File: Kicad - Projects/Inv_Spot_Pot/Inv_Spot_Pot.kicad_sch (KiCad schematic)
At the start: 68 parts, among them J1 Screw_Terminal_01x03, J2 PWM, J3 Display_Power, J4 Current_Sense, Q1 40T120, Q2 40T120, Q3 40T120, Q4 40T120, T1 Transformer_1P_1S, U2 LTV-817S

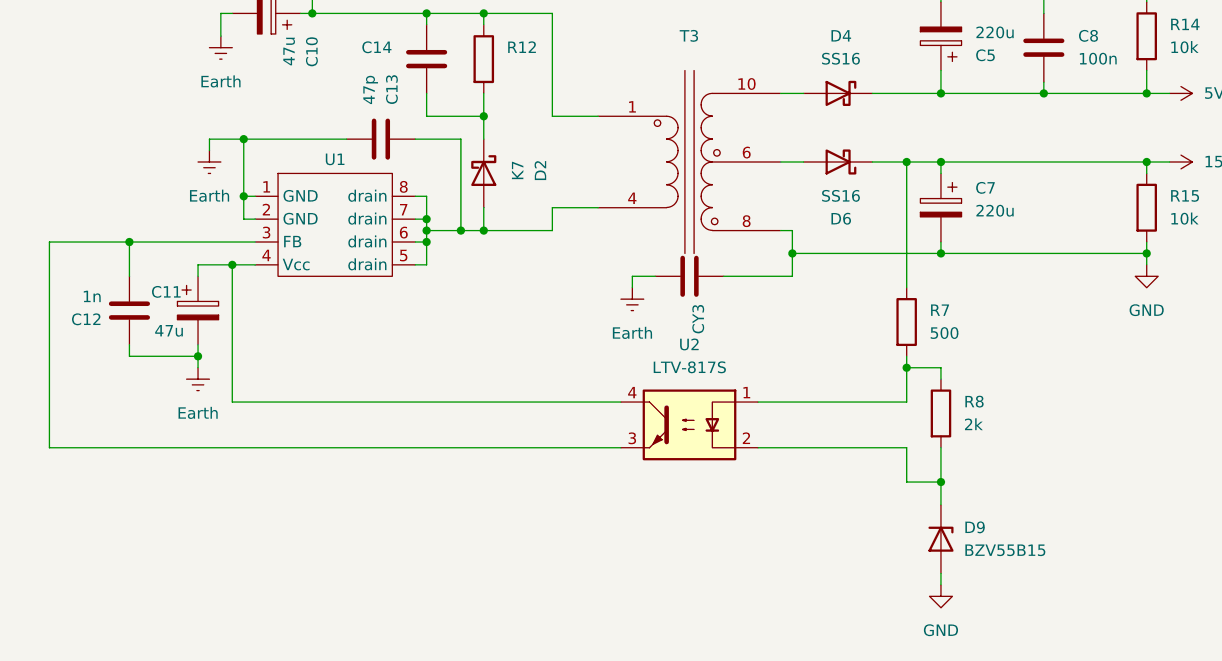
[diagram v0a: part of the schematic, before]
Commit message: Ajuste da PCB
Alargamento das trilhas T- e T+ por meio de zonas de cobre

Ajuste do circuito da fonte auxiliar para uso de zener comum ao invés de TL431
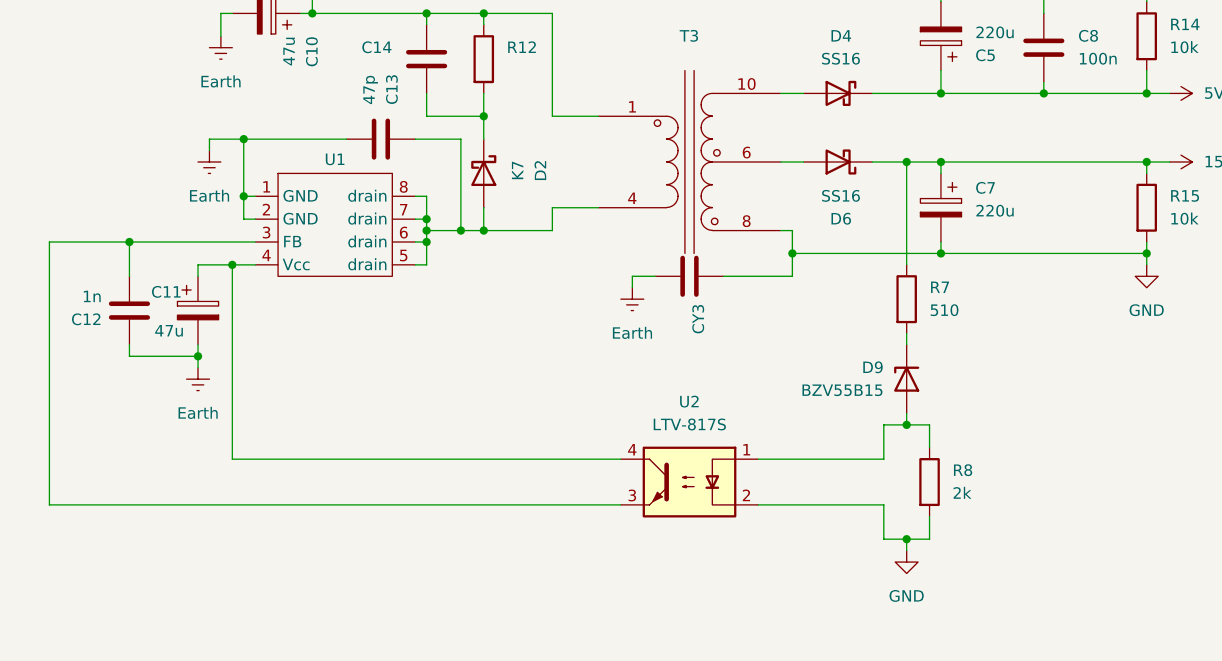
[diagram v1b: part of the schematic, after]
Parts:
- R7: value 500 -> 510
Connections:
- net GND: now also R8.2, U2.2; no longer D9.2 (A)
- net at R8.1, U2.1: now also D9.2 (A); no longer R7.2
- new net: D9.1 (K), R7.2
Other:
- moved on the sheet: D9, R7, R8, U2

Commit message: Atualizações Semi-Finais
Conexão do soft-start e filtro de entrada na placa
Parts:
- removed C10, C11: 47u, Capacitor_THT:CP_Radial_D8.0mm_P3.50mm, symbol Device:C_Polarized
- removed C12: 1n, Capacitor_SMD:C_1206_3216Metric_Pad1.33x1.80mm_HandSolder, symbol Device:C
- removed C13: 47p, Capacitor_THT:C_Disc_D8.0mm_W5.0mm_P7.50mm, symbol Device:C
- removed C14, C8, C9: 100n, Capacitor_SMD:C_1206_3216Metric_Pad1.33x1.80mm_HandSolder, symbol Device:C
- removed C5, C7: 220u, Capacitor_THT:CP_Radial_D8.0mm_P3.50mm, symbol Device:C_Polarized
- removed CY3: C, Capacitor_THT:C_Disc_D10.5mm_W5.0mm_P10.00mm, symbol Device:C
- removed D2: K7, Diode_SMD:D_SMA_Handsoldering, symbol Device:D_Schottky
- removed D4: SS16, Diode_SMD:D_SMA_Handsoldering, symbol Device:D_Schottky
- removed D6: SS16, Diode_SMD:D_SOD-128, symbol Device:D_Schottky
- removed D9: BZV55B15, Diode_SMD:D_MiniMELF, symbol Diode:BZV55B15
- removed F1: Fuse, Fuse:Fuseholder_Clip-5x20mm_Schurter_CQM_Inline_P20.60x5.00mm_D1.00mm_Horizontal, symbol Device:Fuse
- removed F2: Polyfuse, Connector_PinHeader_2.54mm:PinHeader_1x02_P2.54mm_Vertical, symbol Device:Polyfuse
- removed J4: Current_Sense, Connector_PinHeader_2.54mm:PinHeader_1x02_P2.54mm_Vertical, symbol Connector:Conn_01x02_Pin
- removed R12, R8: 2k, Resistor_SMD:R_1206_3216Metric_Pad1.30x1.75mm_HandSolder, symbol Device:R
- removed R14, R15: 10k, Resistor_SMD:R_1206_3216Metric_Pad1.30x1.75mm_HandSolder, symbol Device:R
- removed R7: 510, Resistor_SMD:R_1206_3216Metric_Pad1.30x1.75mm_HandSolder, symbol Device:R
- removed T3: (no value), Transformer_THT:Custom_Transformer-10P-EEL22_EE30_7, symbol Custom_Transformers:Transformer_1P_2S_CT
- removed TR1: TR60_FC, Transformer_THT:Current_Transformer-1_200-21x20, symbol Transformer:TR60_FC
- removed U1: (no value), Package_DIP:DIP-8_W7.62mm_LongPads, symbol Custom_ICs:DK125
- removed U2: LTV-817S, Package_DIP:SMDIP-4_W9.53mm, symbol Isolator:LTV-817S
- added C3, C4: 220u, Capacitor_THT:CP_Radial_D35.0mm_P10.00mm_SnapIn, symbol Device:C_Polarized
- added D10, D11, D12, D13, D14, D15: MUR80G20, Package_TO_SOT_THT:TO-3P-3_Vertical, symbol Device:D_Schottky_Dual_CommonCathode_KAA_Parallel
- added R22: 200k, Resistor_SMD:R_2010_5025Metric, symbol Device:R
- D1: footprint Diode_THT:Diode_Bridge_Vishay_KBU -> Diode_THT:Diode_Bridge_32.0x5.6x17.0mm_P10.0mm_P7.5mm
- J1: footprint TerminalBlock:TerminalBlock_Altech_AK300-3_P5.00mm -> (none)
- R21: footprint Resistor_SMD:R_1206_3216Metric_Pad1.30x1.75mm_HandSolder -> Resistor_SMD:R_2010_5025Metric
- RV1: footprint Varistor:RV_Disc_D21.5mm_W5.6mm_P10mm -> Varistor:RV_Disc_D21.5mm_W4.3mm_P10mm
- renumbered C6 to C2
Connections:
- net 15V: now also J3.1 (Pin_1)
- net 310V: now also C3.1, C4.1, R22.1
- net Earth: now also C3.2, C4.2, R22.2
- net T+: now also T1.1 (AA)
- net T-: now also T1.2 (AB); no longer T1.1 (AA)
- net Soft_Start-24V/~{AC{2}}: now reaches Cx1.1, FL1.1, RV1.1
- net Soft_Start-24V/~{AC{1}}: now reaches Cx1.2, FL1.3, RV1.2
- net Soft_Start-24V/~{AC{1}}: no longer J1.3 (Pin_3)
- net Soft_Start-24V/AC_{1}: now reaches J1.1 (Pin_1)
- new net: D10.2 (A), D11.2 (A), D12.2 (A), D13.2 (A), D14.2 (A), D15.2 (A)
- new net Out1: D10.1 (K), D10.3 (K), D11.1 (K), D11.3 (K), D14.1 (K), D14.3 (K)
- new net Out2: D12.1 (K), D12.3 (K), D13.1 (K), D13.3 (K), D15.1 (K), D15.3 (K)
- new net Soft_Start-24V/AC_{2}: J1.3 (Pin_3)
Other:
- added sheet Power_Supply (PS-5_15.kicad_sch)
- added sheet Soft_Start-24V (Sheets/Soft_Start.kicad_sch)
- moved on the sheet: C1, C15, C16, C17, C18, C2, CY1, CY2, Cx1, Cx2, D1, FL1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

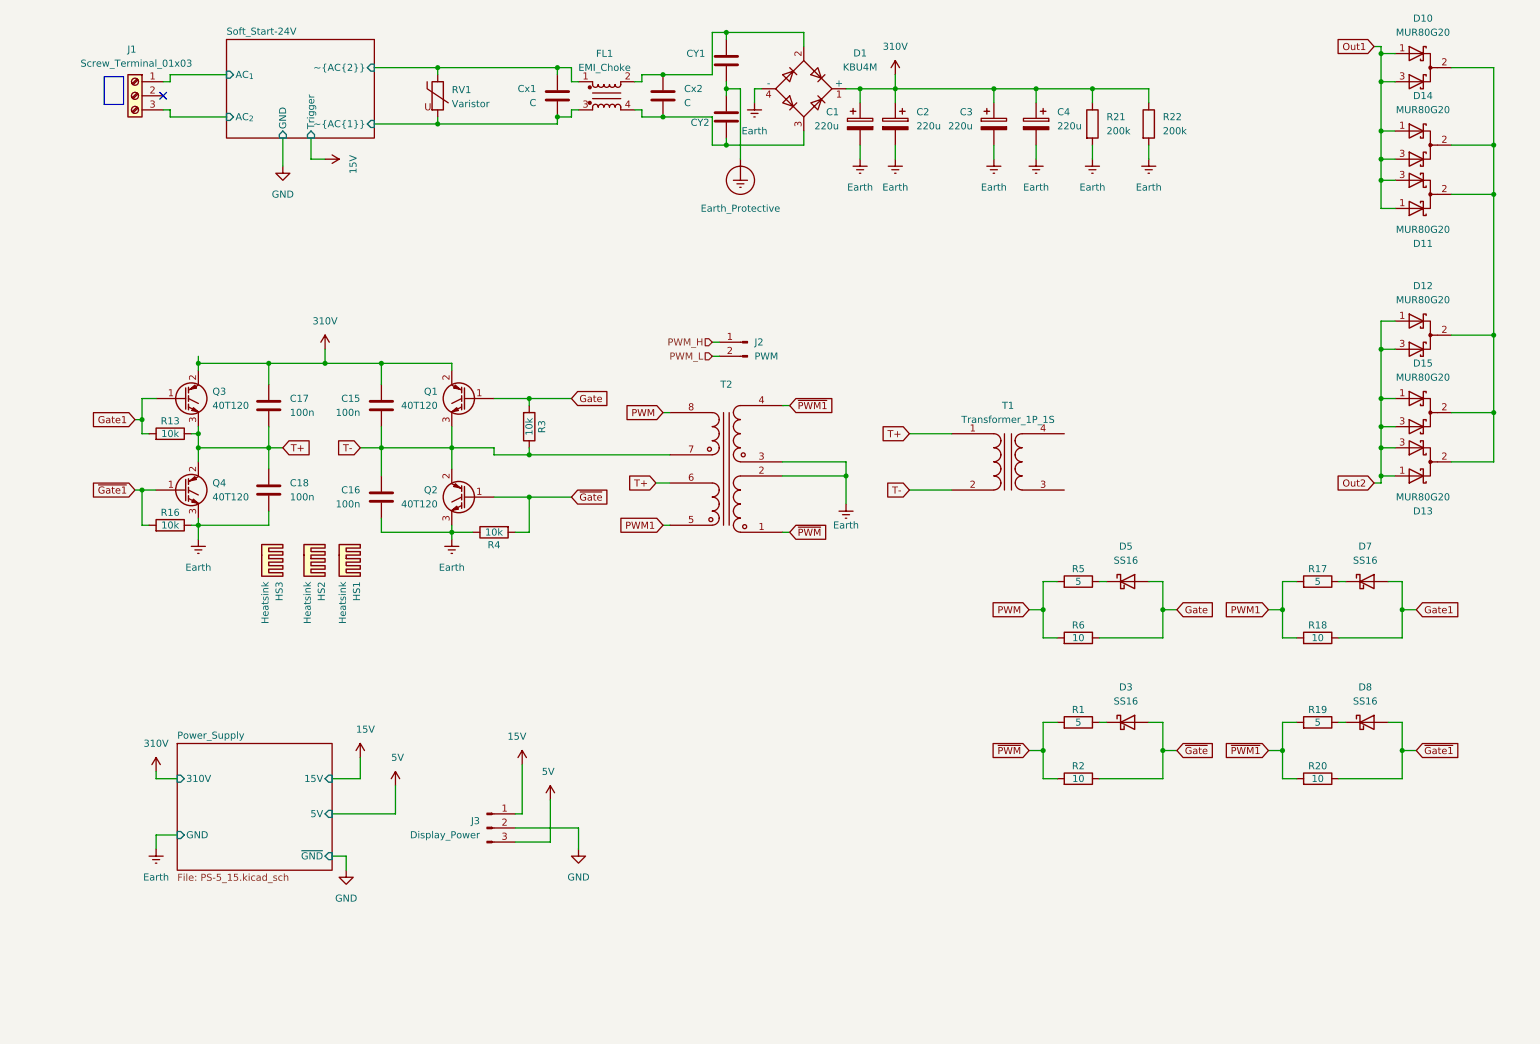
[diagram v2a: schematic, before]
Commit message: Semi-final Touches
Menu now uses power instead of current

Removed pulsed timing from "CARVAO" and "ARRUELA" operation modes

Added parafix mode

Fixed schematic for output transformer

Added rectification on the output

Trying different power trace geometry in antecipation of voltage spikes
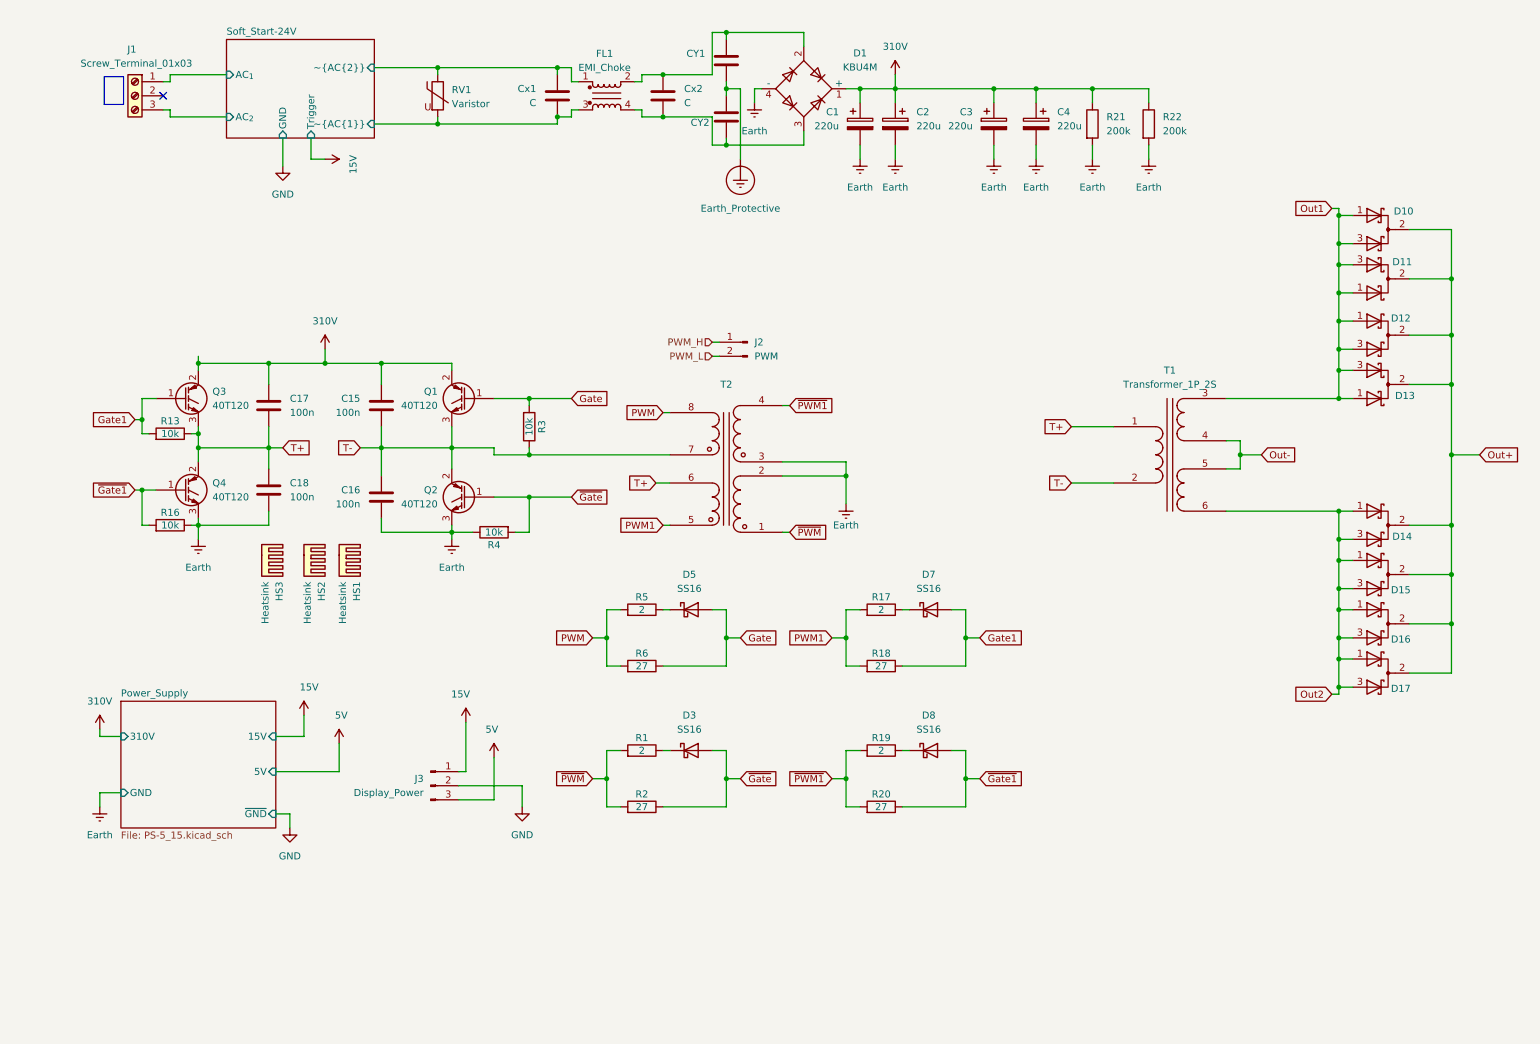
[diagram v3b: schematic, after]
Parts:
- removed T1: Transformer_1P_1S, Transformer_THT:Transformer_Toroid_THT_7032, symbol Device:Transformer_1P_1S
- added D16, D17: MUR80G20, Package_TO_SOT_THT:TO-3P-3_Vertical, symbol Device:D_Schottky_Dual_CommonCathode_KAA_Parallel
- added T1: Transformer_1P_2S, Transformer_THT:Transformer_Toroid_THT_7032, symbol Device:Transformer_1P_2S
- R1, R17, R19, R5: value 5 -> 2
- R18, R2, R20, R6: value 10 -> 27
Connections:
- net Out1: now also D12.1 (K), D12.3 (K), D13.1 (K), D13.3 (K), T1.3 (SA); no longer D14.1 (K), D14.3 (K)
- net Out2: now also D14.1 (K), D14.3 (K), D16.1 (K), D16.3 (K), D17.1 (K), D17.3 (K), T1.6 (SD); no longer D12.1 (K), D12.3 (K), D13.1 (K), D13.3 (K)
- net T+: now also T1.1 (AA)
- net T-: now also T1.2 (AB)
- net Out+: now reaches D10.2 (A), D11.2 (A), D12.2 (A), D13.2 (A), D14.2 (A), D15.2 (A)
- net Out+: now also D16.2 (A), D17.2 (A)
- new net Out-: T1.4 (SB), T1.5 (SC)
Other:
- moved on the sheet: D10, D11, D12, D13, D14, D15, D3, D5, D7, D8, J3, R1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

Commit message: Adicionado Footprint do Transformador
Footprint do transformador adicionada

Linha dos capacitores XY adicionada

Alteração nas linhas de PWM
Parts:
- added C19, C20, C21, C22: 100n, Capacitor_SMD:C_1206_3216Metric_Pad1.33x1.80mm_HandSolder, symbol Device:C
- added J4: 24V, Connector_PinHeader_2.54mm:PinHeader_1x02_P2.54mm_Vertical, symbol Connector:Conn_01x02_Pin
- added J5: Relay_Out, Connector_PinHeader_2.54mm:PinHeader_1x02_P2.54mm_Vertical, symbol Connector:Conn_01x02_Pin
- added J6: Relay_In, Connector_PinHeader_2.54mm:PinHeader_1x02_P2.54mm_Vertical, symbol Connector:Conn_01x02_Pin
- HS2, HS3: footprint Custom_Footprints:Heatsink_17x15mm -> Custom_Heatsink:Floating_28x15x70mm
- T1: footprint Transformer_THT:Transformer_Toroid_THT_7032 -> Custom_Transformer:Transformer_Toroid_THT_7032
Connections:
- net 310V: now also D1.4 (+); no longer D1.1 (+)
- net Earth: now also D1.1 (-), C19.1, C21.2; no longer D1.4 (-)
- net Gate: now also C20.2
- net Gate1: now also C22.1
- net T+: now also C22.2
- net T-: now also C20.1
- net ~{Gate1}: now also C21.1
- net ~{Gate}: now also C19.2
- net at CY1.1, Cx2.1, FL1.2: now also D1.3; no longer D1.2
- net at CY2.2, Cx2.2, FL1.4: now also D1.2; no longer D1.3
- new net 24V: J4.1 (Pin_1), J5.1 (Pin_1), J6.1 (Pin_1)
- new net GND_{24}: J4.2 (Pin_2), J5.2 (Pin_2), J6.2 (Pin_2)
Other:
- sheet Power_Supply: file PS-5_15.kicad_sch -> Sheets/PS-5_15.kicad_sch
- sheet Power_Supply ports: added 24V, GND_{24V}; removed none
- moved on the sheet: R16, R3, R4
